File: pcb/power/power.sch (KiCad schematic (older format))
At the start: 9 parts, among them CON1 BARREL_JACK, P1 CONN_01X04, P2 CONN_01X04, P3 CONN_01X04, P4 USB_A, P5 CONN_01X03, P6 CONN_01X03

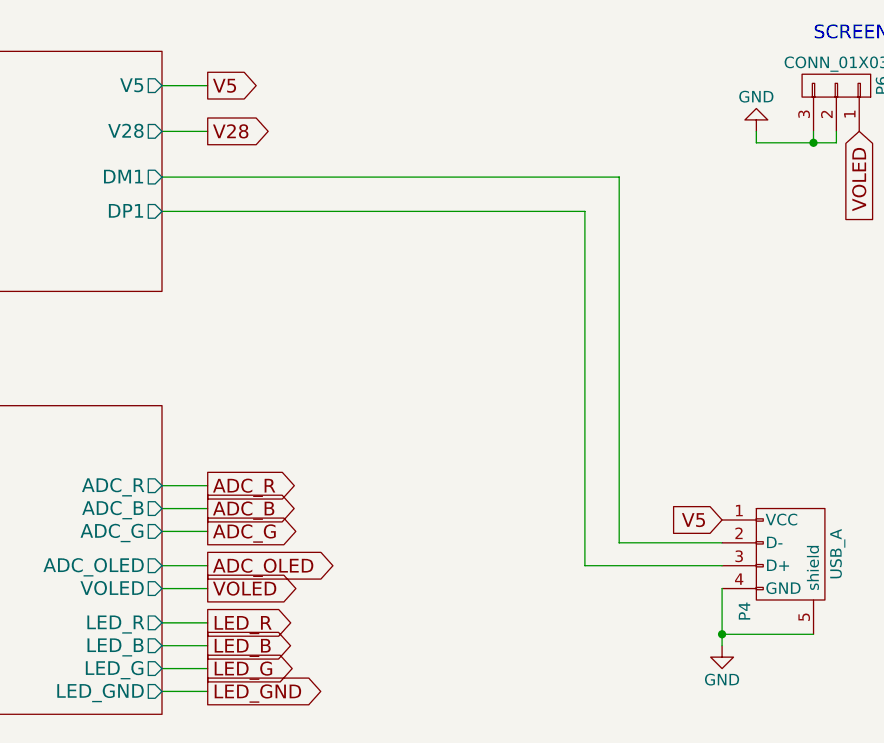
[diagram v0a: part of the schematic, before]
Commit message: Fixed the bug. Now workin with differential amplifiers. Started over once more with the layout.
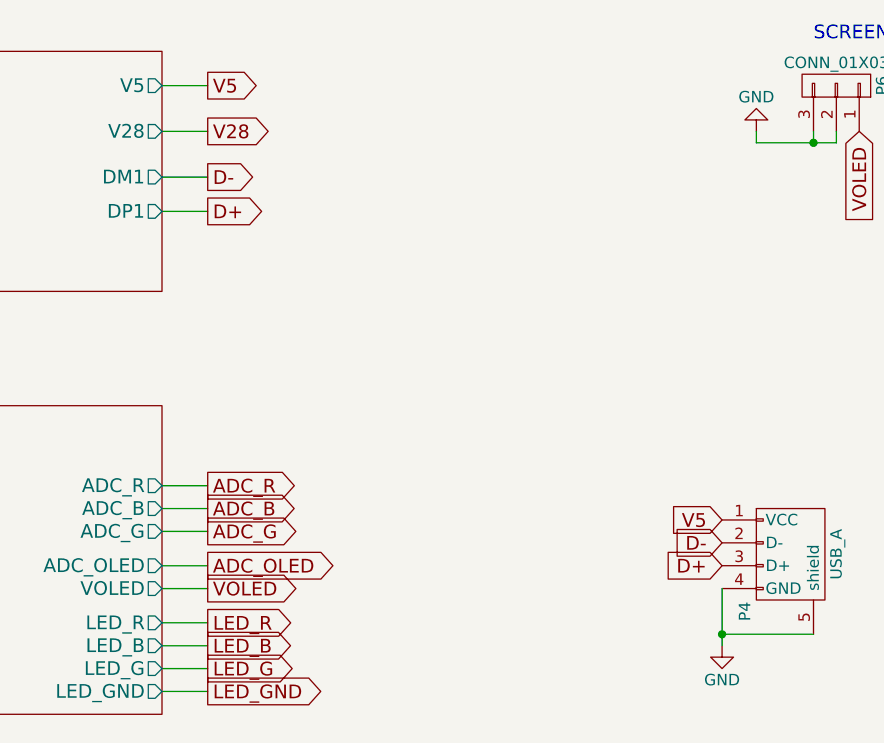
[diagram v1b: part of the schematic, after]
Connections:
- net Bucket Converters/DM1 renamed D-
- net Bucket Converters/DP1 renamed D+
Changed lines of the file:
@@
 Sheet 1 5
 Title "Power Board "
-Date "2016-12-02"
+Date "2016-12-30"
 Rev "1.0"
 Comp "Uppsala University"
@@
 Wire Wire Line
 	7300 1550 7500 1550
-Wire Wire Line
-	7300 1750 9300 1750
-Wire Wire Line
-	9300 1750 9300 3350
-Wire Wire Line
-	9300 3350 9750 3350
-Wire Wire Line
-	9750 3450 9150 3450
-Wire Wire Line
-	9150 3450 9150 1900
-Wire Wire Line
-	9150 1900 7300 1900
+Text GLabel 7500 1750 2    60   Output ~ 0
+D-
+Text GLabel 7500 1900 2    60   Output ~ 0
+D+
+Wire Wire Line
+	7300 1900 7500 1900
+Wire Wire Line
+	7300 1750 7500 1750
+Text GLabel 9750 3350 0    60   Input ~ 0
+D-
+Text GLabel 9750 3450 0    60   Input ~ 0
+D+
 $EndSCHEMATC

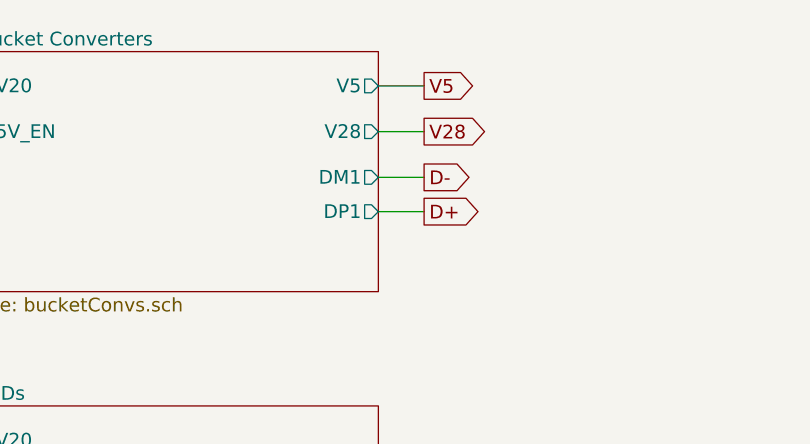
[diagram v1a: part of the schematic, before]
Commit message: Finished the layout almost (third time). Some via stitching still has to be done. Taking a look at heat disipation, too.
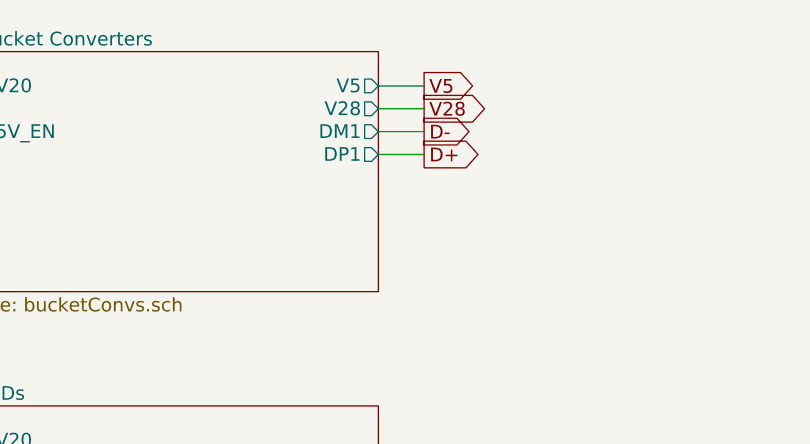
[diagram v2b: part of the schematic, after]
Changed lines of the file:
@@
 F3 "5V_EN" I L 5550 1550 60
 F4 "V5" O R 7300 1350 60
-F5 "V28" O R 7300 1550 60
-F6 "DM1" O R 7300 1750 60
-F7 "DP1" O R 7300 1900 60
+F5 "V28" O R 7300 1450 60
+F6 "DM1" O R 7300 1550 60
+F7 "DP1" O R 7300 1650 60
 $EndSheet
 $Sheet
@@
 Text GLabel 10250 5250 1    60   Input ~ 0
 V28
-Text GLabel 7500 1550 2    60   Output ~ 0
+Text GLabel 7500 1450 2    60   Output ~ 0
 V28
 Text GLabel 7500 1350 2    60   Output ~ 0
@@
 	0    -1   -1   0
 $EndComp
-Wire Wire Line
-	7500 1350 7300 1350
-Wire Wire Line
-	7300 1550 7500 1550
-Text GLabel 7500 1750 2    60   Output ~ 0
+Text GLabel 7500 1550 2    60   Output ~ 0
 D-
-Text GLabel 7500 1900 2    60   Output ~ 0
+Text GLabel 7500 1650 2    60   Output ~ 0
 D+
-Wire Wire Line
-	7300 1900 7500 1900
-Wire Wire Line
-	7300 1750 7500 1750
 Text GLabel 9750 3350 0    60   Input ~ 0
 D-
 Text GLabel 9750 3450 0    60   Input ~ 0
 D+
+Wire Wire Line
+	7300 1650 7500 1650
+Wire Wire Line
+	7500 1550 7300 1550
+Wire Wire Line
+	7300 1450 7500 1450
+Wire Wire Line
+	7500 1350 7300 1350
 $EndSCHEMATC

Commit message: Fixed a bug.
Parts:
- R1: Digikey 311-10.0KHRCT-ND -> 311-10KGRCT-ND
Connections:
- net LED_B: now also P3.2 (P2); no longer P3.3 (P3)
- net LED_G: now also P3.3 (P3); no longer P3.2 (P2)
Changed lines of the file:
@@
 PWM_R
 $Comp
-L GND #PWR4
+L GND #PWR01
 U 1 1 583EB242
 P 9900 1550
-F 0 "#PWR4" H 9900 1300 50  0001 C CNN
+F 0 "#PWR01" H 9900 1300 50  0001 C CNN
 F 1 "GND" H 9900 1400 50  0000 C CNN
 F 2 "" H 9900 1550 50  0000 C CNN
@@
 $EndComp
 $Comp
-L GND #PWR1
+L GND #PWR02
 U 1 1 583C8E04
 P 1650 4350
-F 0 "#PWR1" H 1650 4100 50  0001 C CNN
+F 0 "#PWR02" H 1650 4100 50  0001 C CNN
 F 1 "GND" H 1650 4200 50  0000 C CNN
 F 2 "" H 1650 4350 50  0000 C CNN
@@
 F 2 "Additional:R_0603_HandSoldering_Same_As_C" V 2230 4100 50  0001 C CNN
 F 3 "http://www.yageo.com.tw/exep/pages/download/literatures/PYu-R_INT-thick_7.pdf" H 2300 4100 50  0001 C CNN
-F 4 " 311-10.0KHRCT-ND" V 2300 4100 60  0001 C CNN "Digikey"
+F 4 "311-10KGRCT-ND" V 2300 4100 60  0001 C CNN "Digikey"
 	1    2300 4100
 	1    0    0    -1
@@
 V20
 $Comp
-L PWR_FLAG #FLG2
+L PWR_FLAG #FLG03
 U 1 1 58428672
 P 2300 3350
-F 0 "#FLG2" H 2300 3445 50  0001 C CNN
+F 0 "#FLG03" H 2300 3445 50  0001 C CNN
 F 1 "PWR_FLAG" H 2300 3530 50  0000 C CNN
 F 2 "" H 2300 3350 50  0000 C CNN
@@
 $EndComp
 $Comp
-L PWR_FLAG #FLG1
+L PWR_FLAG #FLG04
 U 1 1 5842A47B
 P 1950 4200
-F 0 "#FLG1" H 1950 4295 50  0001 C CNN
+F 0 "#FLG04" H 1950 4295 50  0001 C CNN
 F 1 "PWR_FLAG" H 1950 4380 50  0000 C CNN
 F 2 "" H 1950 4200 50  0000 C CNN
@@
 	5400 5500 5550 5500
 $Comp
-L GND #PWR3
+L GND #PWR05
 U 1 1 58444C94
 P 9800 5250
-F 0 "#PWR3" H 9800 5000 50  0001 C CNN
+F 0 "#PWR05" H 9800 5000 50  0001 C CNN
 F 1 "GND" H 9800 5100 50  0000 C CNN
 F 2 "" H 9800 5250 50  0000 C CNN
@@
 V5
 $Comp
-L GND #PWR2
+L GND #PWR06
 U 1 1 58446B04
 P 9750 3800
-F 0 "#PWR2" H 9750 3550 50  0001 C CNN
+F 0 "#PWR06" H 9750 3550 50  0001 C CNN
 F 1 "GND" H 9750 3650 50  0000 C CNN
 F 2 "" H 9750 3800 50  0000 C CNN
@@
 Text GLabel 3450 1600 3    60   Input ~ 0
 LED_R
+Text GLabel 3250 1600 3    60   Input ~ 0
+LED_B
 Text GLabel 3350 1600 3    60   Input ~ 0
-LED_B
-Text GLabel 3250 1600 3    60   Input ~ 0
 LED_G
 Text GLabel 3150 1600 3    60   Input ~ 0
 LED_GND
+Text GLabel 7500 1550 2    60   Output ~ 0
+D-
+Text GLabel 7500 1650 2    60   Output ~ 0
+D+
+Text GLabel 9750 3350 0    60   Input ~ 0
+D-
+Text GLabel 9750 3450 0    60   Input ~ 0
+D+
+Wire Wire Line
+	7300 1650 7500 1650
+Wire Wire Line
+	7500 1550 7300 1550
+Wire Wire Line
+	7300 1450 7500 1450
+Wire Wire Line
+	7500 1350 7300 1350
 $Comp
 L CONN_01X04 P3
@@
 	0    -1   -1   0
 $EndComp
-Text GLabel 7500 1550 2    60   Output ~ 0
-D-
-Text GLabel 7500 1650 2    60   Output ~ 0
-D+
-Text GLabel 9750 3350 0    60   Input ~ 0
-D-
-Text GLabel 9750 3450 0    60   Input ~ 0
-D+
-Wire Wire Line
-	7300 1650 7500 1650
-Wire Wire Line
-	7500 1550 7300 1550
-Wire Wire Line
-	7300 1450 7500 1450
-Wire Wire Line
-	7500 1350 7300 1350
 $EndSCHEMATC

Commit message: Minor changes.
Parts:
- D1: symbol LED -> LED-RESCUE-power
- P4: symbol USB_A -> USB_A-RESCUE-power
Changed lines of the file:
@@
 EESchema Schematic File Version 2
+LIBS:power-rescue
 LIBS:power
 LIBS:device
@@
 VOLED
 $Comp
-L LED D1
+L LED-RESCUE-power D1
 U 1 1 583D79A8
 P 2300 3700
@@
 $EndSheet
 $Comp
-L USB_A P4
+L USB_A-RESCUE-power P4
 U 1 1 584373B8
 P 10050 3450
